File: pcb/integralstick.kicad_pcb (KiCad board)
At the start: 4 copper layers, 235 parts, among them J1 CONN_INTEGRALSTICK_FPGA_DEVICE, J2 CONN_INTEGRALSTICK_MCU_DEVICE, Q1 SSM6N58NU, Q2 SSM6N58NU, Q3 SSM6N58NU, U1 STM32F777NIH6‎, U10 DSC6083MI2A-032K768, U12 DSC6001HI2A-025.0000‎, U2 XC7A50T-1FTG256C, U3 S27KS0641, U4 S27KS0641, U5 KSZ9031RN, U6 S25FL064LABNFI011‎, U7 LTC3374-QFN, U8 DSC6001HI2A-025.0000, U9 AT24MAC402-UDFN

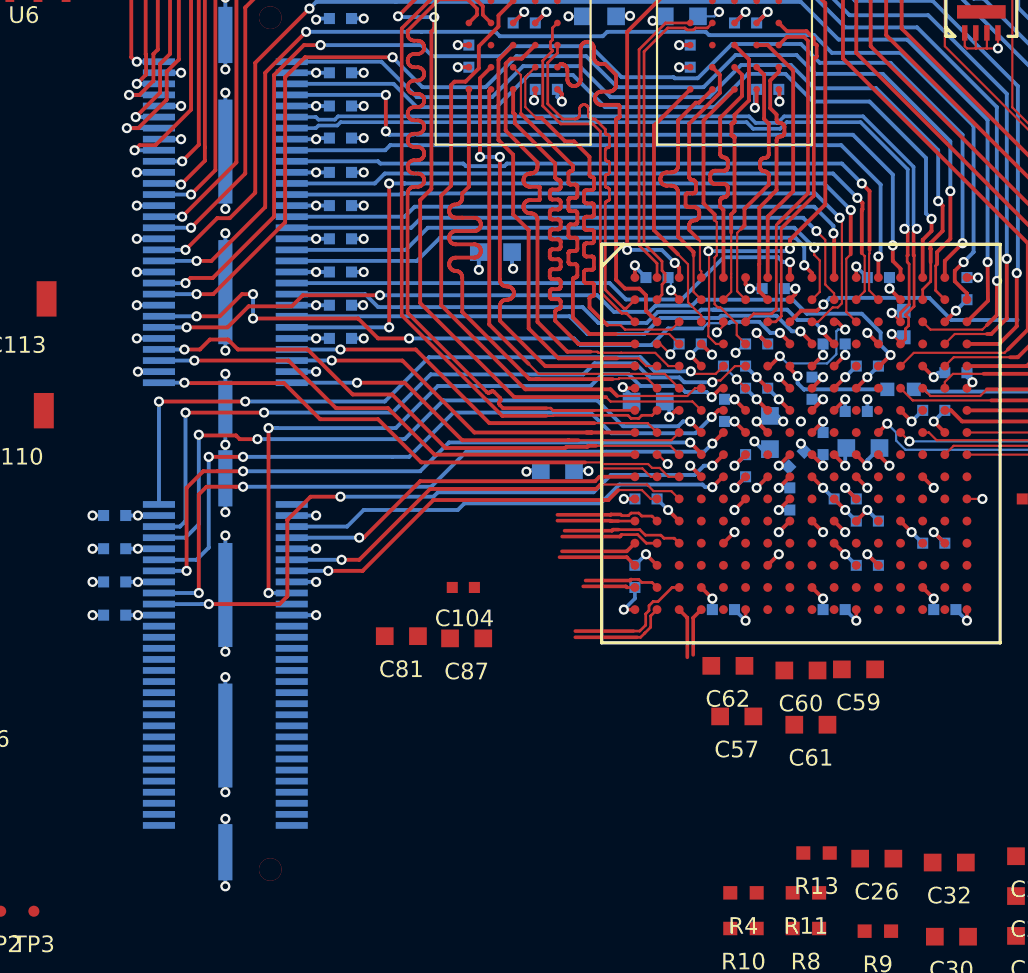
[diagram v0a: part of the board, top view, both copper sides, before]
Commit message: Initial layout of LVDS bank
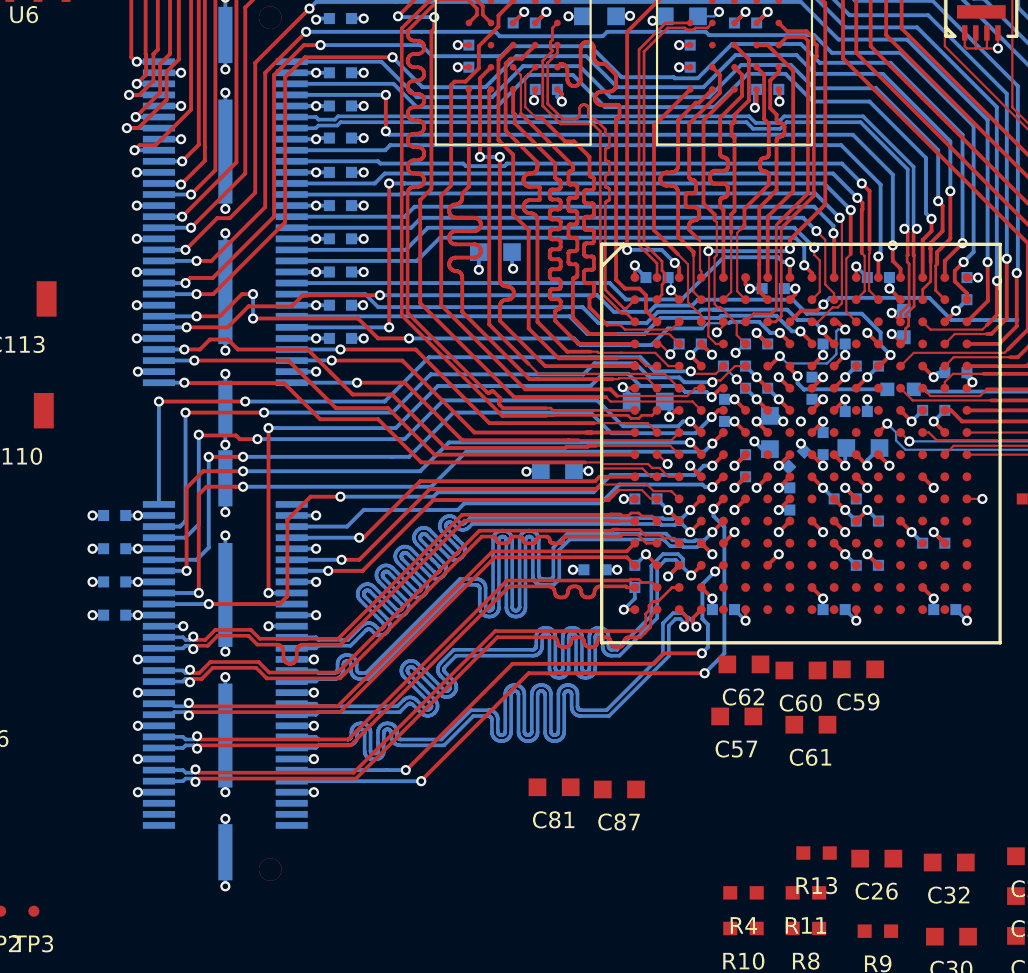
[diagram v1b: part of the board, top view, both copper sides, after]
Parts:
- C104: moved to B.Cu
- moved C87 9.71 mm to (55.8, 58.6)
- moved C81 9.71 mm to (52.9, 58.5)
- moved C104 6.00 mm to (54.7, 48.7)
- moved C62 0.73 mm to (61.4, 53.0)
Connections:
- J1 pad 10: /FPGA/LVDS_DQ4_N -> /FPGA/LVDS_DQ8_N
- J1 pad 11: /FPGA/LVDS_DQ2_P -> /FPGA/GPIO_2V5_0
- J1 pad 12: /FPGA/LVDS_DQ2_N -> /FPGA/LVDS_DQ8_P
- J1 pad 15: /FPGA/LVDS_DQ8_P -> /FPGA/LVDS_DQ7_N
- J1 pad 16: /FPGA/GPIO_2V5_0 -> /FPGA/LVDS_DQ6_N
- J1 pad 17: /FPGA/LVDS_DQ8_N -> /FPGA/LVDS_DQ7_P
- J1 pad 18: /FPGA/GPIO_2V5_1 -> /FPGA/LVDS_DQ6_P
- J1 pad 2: /2V5 -> /Power Supply/5V0
- J1 pad 21: /FPGA/LVDS_DQ6_P -> /FPGA/LVDS_DQ5_N
- J1 pad 22: /FPGA/LVDS_DQ5_P -> /FPGA/LVDS_DQ4_N
- J1 pad 23: /FPGA/LVDS_DQ6_N -> /FPGA/LVDS_DQ5_P
- J1 pad 24: /FPGA/LVDS_DQ5_N -> /FPGA/LVDS_DQ4_P
- J1 pad 25: /1V8 -> /2V5
- J1 pad 27: /FPGA/LVDS_DQ7_P -> /FPGA/LVDS_DQ3_N
- J1 pad 28: /FPGA/LVDS_DQ7_N -> /FPGA/LVDS_DQ2_N
- J1 pad 29: /FPGA/LVDS_DQ3_N -> /FPGA/LVDS_DQ3_P
- J1 pad 3: /2V5 -> /Power Supply/5V0
- J1 pad 30: /FPGA/LVDS_DQ3_P -> /FPGA/LVDS_DQ2_P
- J1 pad 33: /1V8 -> /FPGA/LVDS_DQ1_N
- J1 pad 34: /2V5 -> /FPGA/LVDS_DQ0_N
- J1 pad 35: /FPGA/LVDS_DQ0_P -> /FPGA/LVDS_DQ1_P
- J1 pad 36: /FPGA/LVDS_DQ1_P -> /FPGA/LVDS_DQ0_P
- J1 pad 37: /FPGA/LVDS_DQ0_N -> /2V5
- J1 pad 38: /FPGA/LVDS_DQ1_N -> /2V5
- J1 pad 9: /FPGA/LVDS_DQ4_P -> /FPGA/GPIO_2V5_1
- U2 pad L4: /FPGA/LVDS_DQ0_P -> /FPGA/LVDS_DQ1_P
- U2 pad L5: /FPGA/GPIO_2V5_0 -> /FPGA/GPIO_2V5_1
- U2 pad M1: /FPGA/LVDS_DQ1_N -> /FPGA/LVDS_DQ0_N
- U2 pad M2: /FPGA/LVDS_DQ1_P -> /FPGA/LVDS_DQ0_P
- U2 pad M4: /FPGA/LVDS_DQ0_N -> /FPGA/LVDS_DQ1_N
- U2 pad M5: /FPGA/LVDS_DQ5_P -> /FPGA/LVDS_DQ3_P
- U2 pad N1: /FPGA/LVDS_DQ3_P -> /FPGA/LVDS_DQ4_P
- U2 pad N4: /FPGA/LVDS_DQ5_N -> /FPGA/LVDS_DQ3_N
- U2 pad P1: /FPGA/LVDS_DQ3_N -> /FPGA/LVDS_DQ4_N
- U2 pad P3: /FPGA/LVDS_DQ4_N -> /FPGA/LVDS_DQ5_N
- U2 pad P4: /FPGA/LVDS_DQ4_P -> /FPGA/LVDS_DQ5_P
- U2 pad P5: /FPGA/GPIO_2V5_1 -> /FPGA/GPIO_2V5_0
- U2 pad R3: /FPGA/LVDS_DQ7_P -> /FPGA/LVDS_DQ8_P
- U2 pad T2: /FPGA/LVDS_DQ7_N -> /FPGA/LVDS_DQ8_N
- U2 pad T3: /FPGA/LVDS_DQ8_N -> /FPGA/LVDS_DQ7_N
- U2 pad T4: /FPGA/LVDS_DQ8_P -> /FPGA/LVDS_DQ7_P
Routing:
- net /2V5: track 12.5 -> 50.6 mm, vias 3 -> 16
- net /FPGA/LVDS_DQ5_P: track 0.00 -> 37.8 mm, vias 0 -> 1
- net /FPGA/LVDS_DQ5_N: track 0.00 -> 37.5 mm, vias 0 -> 1
- net /FPGA/LVDS_DQ3_P: track 3.45 -> 37.8 mm, vias 0 -> 1
- net /FPGA/LVDS_DQ3_N: track 3.56 -> 37.8 mm, vias 0 -> 1
- net /FPGA/LVDS_DQ1_N: track 3.51 -> 37.7 mm, vias 0 -> 1
- net /FPGA/LVDS_DQ1_P: track 4.73 -> 37.7 mm, vias 0 -> 1
- net /FPGA/LVDS_DQ7_N: track 4.51 -> 37.3 mm, vias 0 -> 1
- net /FPGA/LVDS_DQ7_P: track 5.94 -> 37.8 mm, vias 0 -> 1
- net /FPGA/GPIO_2V5_1: track 0.00 -> 29.3 mm, vias 0 -> 3
- net /FPGA/LVDS_DQ0_N: track 0.00 -> 25.6 mm, vias 0 -> 1
- net /FPGA/LVDS_DQ0_P: track 0.00 -> 25.6 mm, vias 0 -> 1
- net /FPGA/LVDS_DQ8_P: track 2.20 -> 27.6 mm, vias 0 -> 1
- net /FPGA/GPIO_2V5_0: track 0.00 -> 25.4 mm, vias 0 -> 3
- net /FPGA/LVDS_DQ8_N: track 2.31 -> 27.6 mm, vias 0 -> 1
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
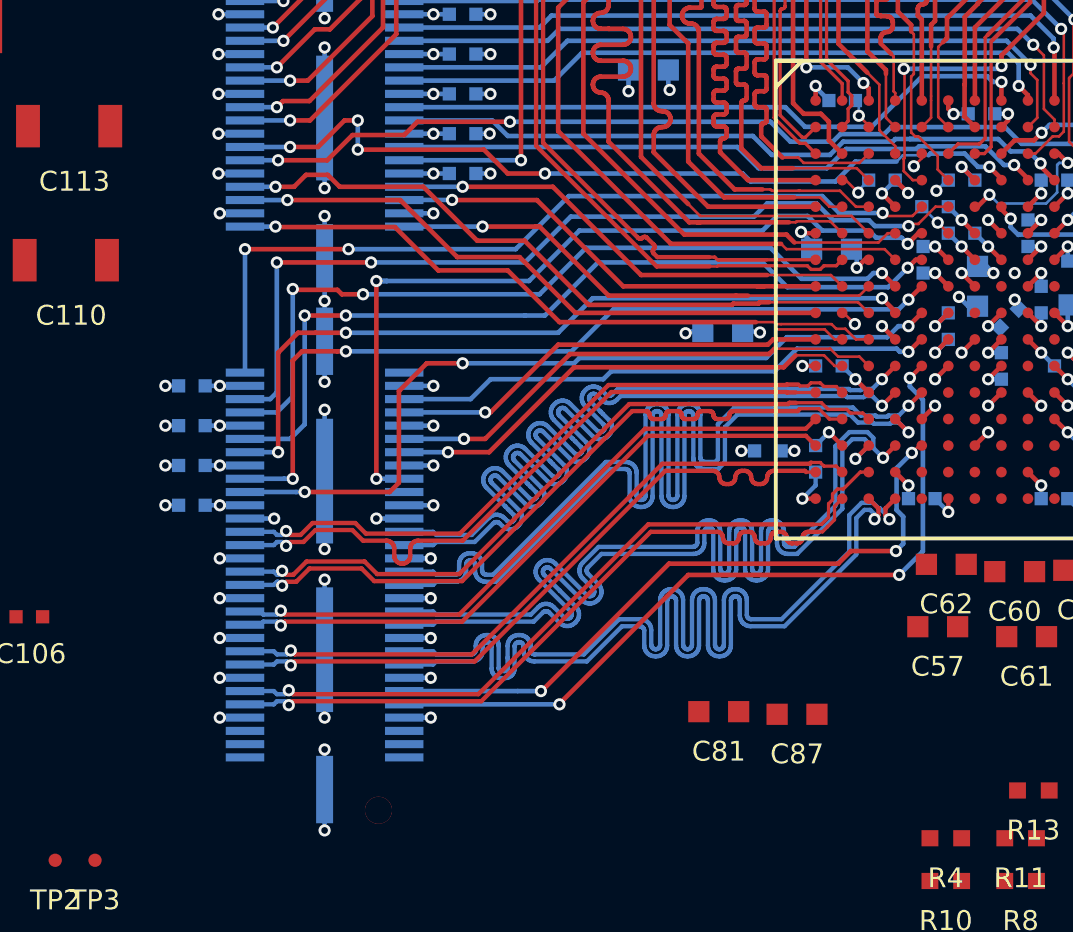
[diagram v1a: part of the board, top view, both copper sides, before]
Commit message: Added missing 1V8 clock. Tweaked planes. Added some layer change caps.
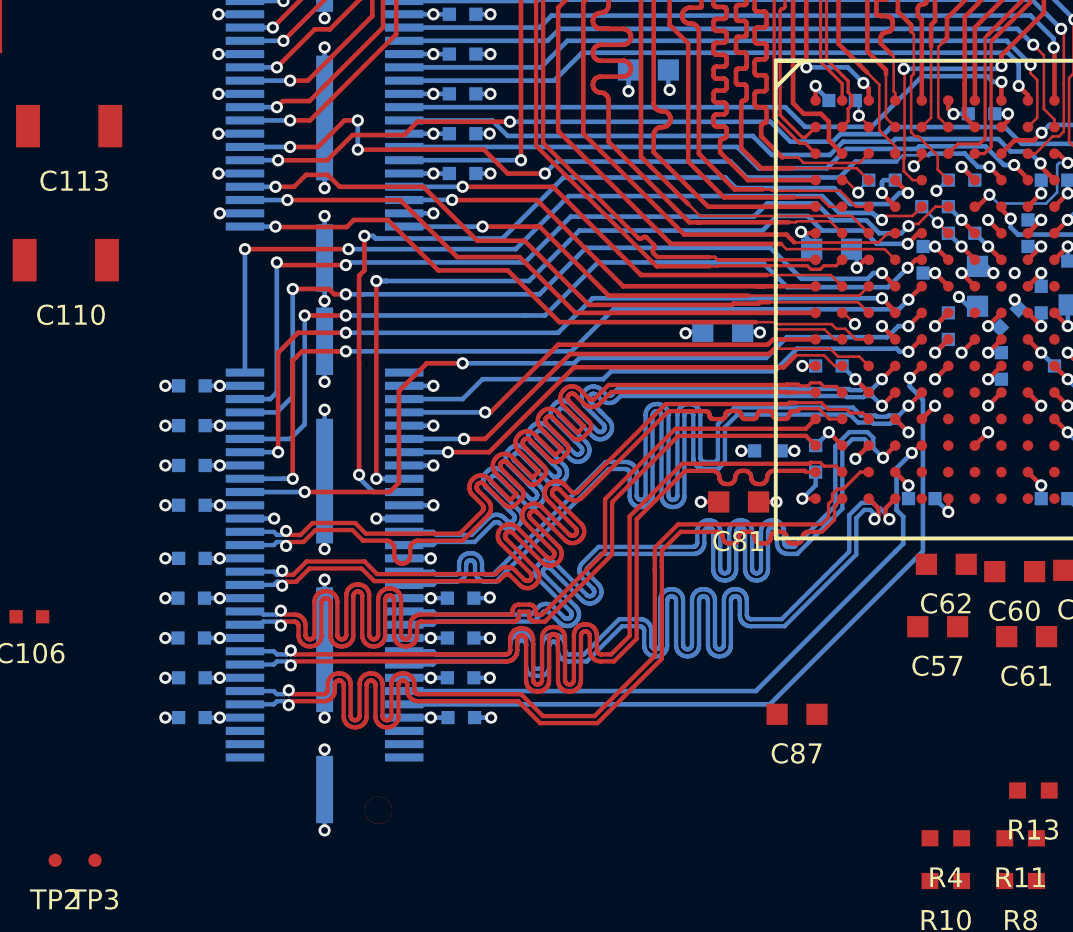
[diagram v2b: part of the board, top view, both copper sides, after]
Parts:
- added C135: 0.47 uF, azonenberg_pcb:EIA_0402_CAP_NOSILK, B.Cu at (33.0, 55.8)
- added C136: 0.47 uF, azonenberg_pcb:EIA_0402_CAP_NOSILK, B.Cu at (33.0, 54.2)
- added C137: 0.47 uF, azonenberg_pcb:EIA_0402_CAP_NOSILK, B.Cu at (33.0, 52.8)
- added C138: 0.47 uF, azonenberg_pcb:EIA_0402_CAP_NOSILK, B.Cu at (33.0, 57.2)
- added C139: 0.47 uF, azonenberg_pcb:EIA_0402_CAP_NOSILK, B.Cu at (33.0, 58.8)
- added C140: 0.47 uF, azonenberg_pcb:EIA_0402_CAP_NOSILK, B.Cu at (43.1, 58.8)
- added C141: 0.47 uF, azonenberg_pcb:EIA_0402_CAP_NOSILK, B.Cu at (43.1, 57.2)
- added C142: 0.47 uF, azonenberg_pcb:EIA_0402_CAP_NOSILK, B.Cu at (43.1, 55.8)
- added C143: 0.47 uF, azonenberg_pcb:EIA_0402_CAP_NOSILK, B.Cu at (43.1, 54.2)
- moved C81 7.94 mm to (53.6, 50.6)
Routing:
- net /RAM/CLK_1V8_1: track 0.68 -> 33.9 mm, vias 1 -> 3
- net /GND: track 385.9 -> 413.0 mm, vias 90 -> 100
- net /2V5: track 50.6 -> 70.6 mm, vias 16 -> 17
- net /FPGA/LVDS_DQ4_P: track 24.7 -> 37.9 mm
- net /FPGA/LVDS_DQ4_N: track 24.7 -> 37.9 mm
- net /FPGA/LVDS_DQ0_P: track 25.6 -> 37.8 mm
- net /FPGA/LVDS_DQ0_N: track 25.6 -> 37.8 mm
- net /FPGA/LVDS_DQ6_P: track 25.8 -> 37.8 mm
- net /FPGA/LVDS_DQ6_N: track 25.8 -> 37.8 mm
- net /FPGA/LVDS_DQ2_N: track 27.0 -> 37.8 mm
- net /FPGA/LVDS_DQ2_P: track 27.0 -> 37.8 mm
- net /FPGA/LVDS_DQ8_N: track 27.6 -> 37.8 mm
- net /FPGA/LVDS_DQ8_P: track 27.6 -> 37.8 mm
- net /FPGA/GPIO_2V5_1: vias 3 -> 1
- net /FPGA/GPIO_2V5_0: vias 3 -> 1

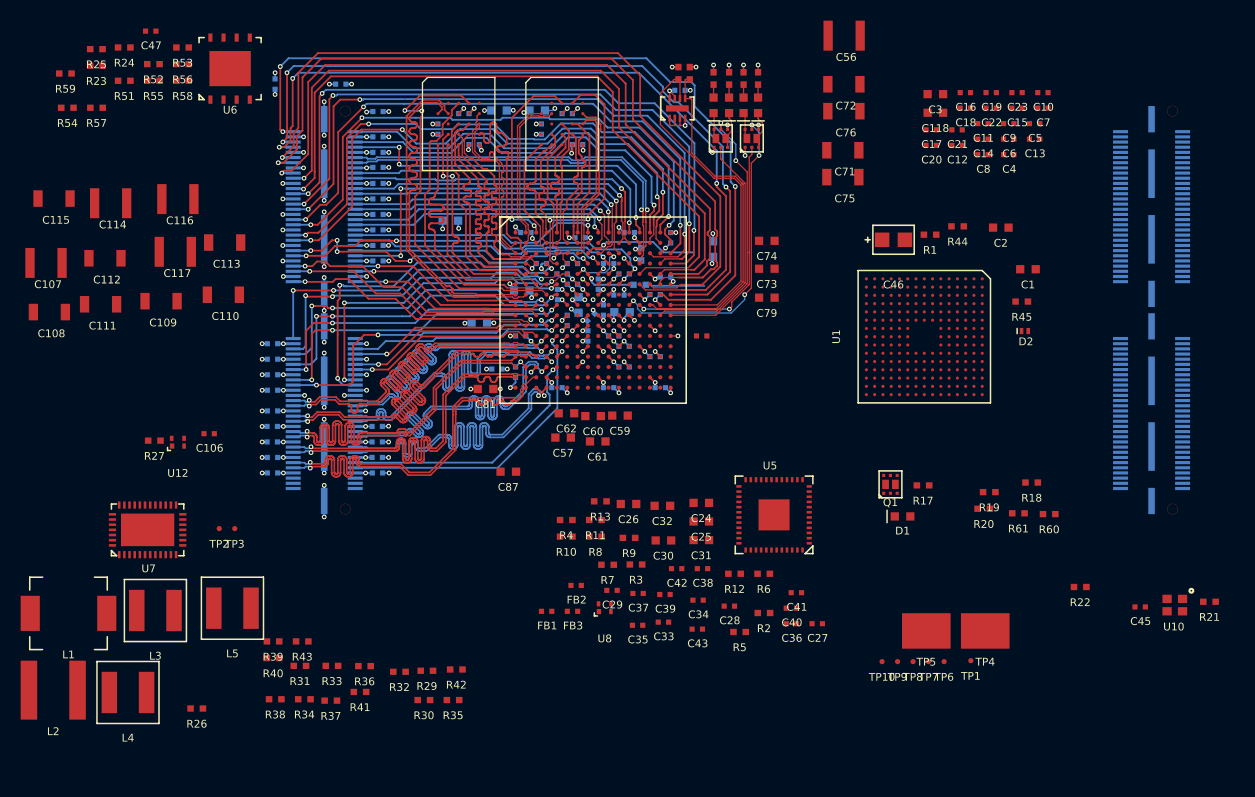
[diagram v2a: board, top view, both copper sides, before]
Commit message: Continued FPGA layout. Fanned out most signals going to MCU but pin assignments aren't final.
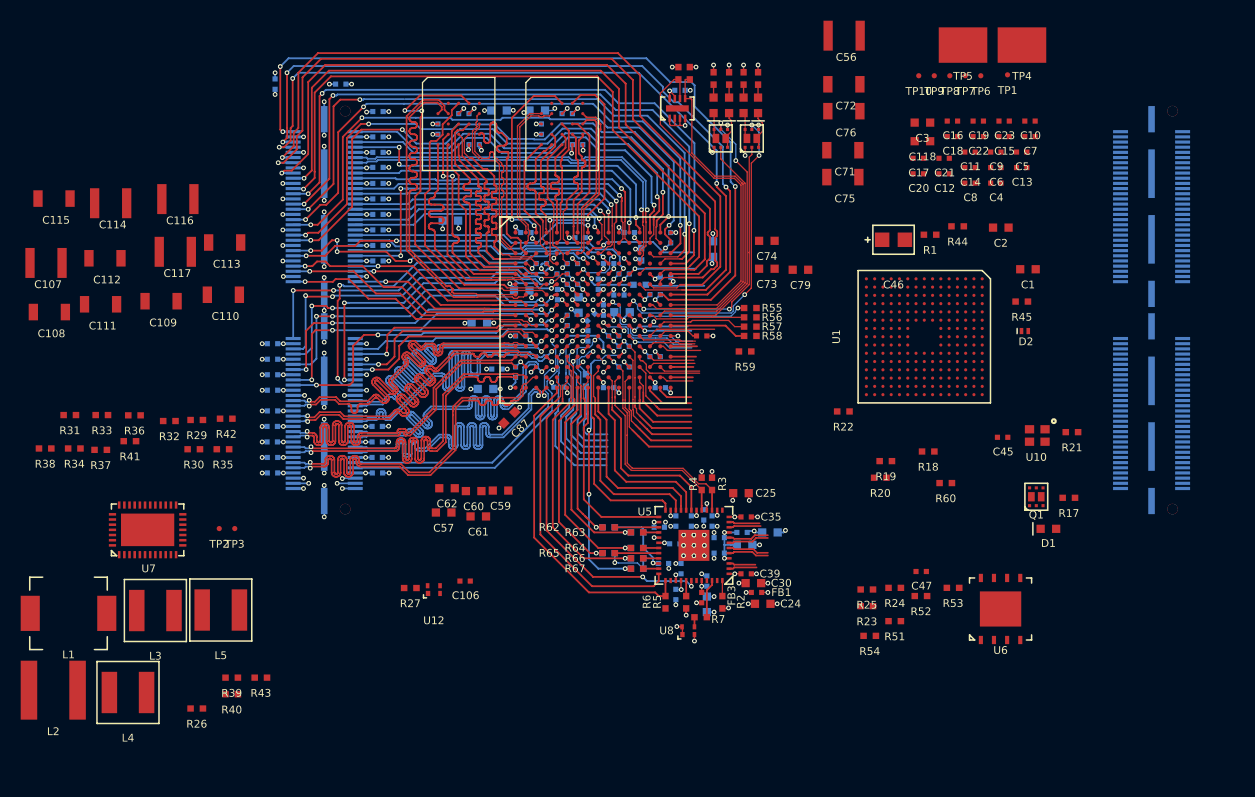
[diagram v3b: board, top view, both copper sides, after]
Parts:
- added R62: 33, azonenberg_pcb:EIA_0402_RES_NOSILK, F.Cu at (65.5, 64.0)
- added R63: 33, azonenberg_pcb:EIA_0402_RES_NOSILK, F.Cu at (68.2, 64.5)
- added R64: 33, azonenberg_pcb:EIA_0402_RES_NOSILK, F.Cu at (68.2, 66.0)
- added R65: 33, azonenberg_pcb:EIA_0402_RES_NOSILK, F.Cu at (65.5, 66.5)
- added R66: 33, azonenberg_pcb:EIA_0402_RES_NOSILK, F.Cu at (68.2, 67.0)
- added R67: 33, azonenberg_pcb:EIA_0402_RES_NOSILK, F.Cu at (68.2, 68.0)
- C26, C27, C28, C29, C31, C32, C33, C34, C36, C37, C38, C40, C41, C42, C43, C81, FB2, R10, R11, R12, R13, R61, R8, R9: moved to B.Cu
- moved R54 92.9 mm to (90.8, 74.5)
- moved C47 91.0 mm to (95.7, 68.3)
- moved R23 91.0 mm to (90.5, 71.6)
- moved R24 91.0 mm to (93.2, 69.9)
- moved R25 91.0 mm to (90.5, 70.0)
- moved R51 91.0 mm to (93.2, 73.1)
- moved R53 91.0 mm to (98.8, 69.9)
- moved U6 91.0 mm to (103.4, 71.9)
- moved R52 90.3 mm to (95.7, 70.7)
- moved R59 71.0 mm to (78.7, 47.0)
- moved R57 66.7 mm to (79.2, 44.6)
- moved R55 61.8 mm to (79.2, 42.8)
- moved R58 60.2 mm to (79.2, 45.5)
- moved R56 60.1 mm to (79.2, 43.7)
- moved TP1 56.8 mm to (104.1, 20.2)
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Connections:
- U2 pad E11: /FPGA/FPGA_CLK_25MHZ -> /FPGA/CLK_3V3_1
- U2 pad E12: /FPGA/CLK_3V3_1 -> /FPGA/FPGA_CLK_25MHZ
- U2 pad M6: /Ethernet/RGMII_TXD2 -> /MCU/DCMI_D7
- U2 pad N11: /MCU/RMII_REFCLK -> /Ethernet/RGMII_RX_CLK
- U2 pad N12: /Ethernet/RGMII_MDC -> /MCU/SPI5_SCK
- U2 pad N13: /Ethernet/RGMII_RXD2 -> /MCU/DCMI_D0
- U2 pad N14: /Ethernet/RGMII_RX_CLK -> /MCU/RMII_REFCLK
- U2 pad N6: /Ethernet/RGMII_TXD1 -> /Ethernet/RGMII_RXD0
- U2 pad P10: /Ethernet/RGMII_RST_N -> /MCU/DCMI_D4
- U2 pad P11: /ETH_LED1_N -> /ETH_LED2_N
- U2 pad P13: /Ethernet/RGMII_RXD3 -> /MCU/DCMI_D2
- U2 pad P14: /Ethernet/RGMII_RX_DV -> /MCU/DCMI_D3
- U2 pad P15: /Ethernet/RGMII_MDIO -> /MCU/DCMI_D1
- U2 pad P6: /MCU/DCMI_D7 -> /Ethernet/RGMII_RX_DV
- U2 pad P8: /Ethernet/RGMII_TXD0 -> /Ethernet/RGMII_TX_CLK
- U2 pad R10: Net-(R22-Pad1) -> /Ethernet/RGMII_TXD0
- U2 pad R11: /MCU/SPI5_SCK -> /ETH_LED1_N
- U2 pad R12: /ETH_LED2_N -> /MCU/DCMI_PIXCLK
- U2 pad R16: /MCU/DCMI_PIXCLK -> Net-(R22-Pad1)
- U2 pad R5: /MCU/DCMI_D3 -> /Ethernet/RGMII_MDC
- U2 pad R6: /MCU/DCMI_D5 -> /Ethernet/RGMII_RST_N
- U2 pad R7: /MCU/DCMI_D6 -> /Ethernet/RGMII_RXD2
- U2 pad R8: /Ethernet/RGMII_TX_EN -> /Ethernet/RGMII_RXD3
- U2 pad T10: /MCU/DCMI_D2 -> /Ethernet/RGMII_TXD1
- U2 pad T14: /Ethernet/RGMII_RXD0 -> /MCU/DCMI_D6
- U2 pad T15: /Ethernet/RGMII_RXD1 -> /MCU/DCMI_D5
- U2 pad T5: /MCU/DCMI_D4 -> /Ethernet/RGMII_MDIO
- U2 pad T7: /Ethernet/RGMII_TX_CLK -> /Ethernet/RGMII_RXD1
- U2 pad T8: /MCU/DCMI_D0 -> /Ethernet/RGMII_TX_EN
- U2 pad T9: /MCU/DCMI_D1 -> /Ethernet/RGMII_TXD2
- U5 pad 27: /Ethernet/RGMII_RXD3 -> Net-(R62-Pad2)
- U5 pad 28: /Ethernet/RGMII_RXD2 -> Net-(R63-Pad2)
- U5 pad 31: /Ethernet/RGMII_RXD1 -> Net-(R64-Pad2)
- U5 pad 32: /Ethernet/RGMII_RXD0 -> Net-(R65-Pad2)
- U5 pad 33: /Ethernet/RGMII_RX_DV -> Net-(R66-Pad2)
- U5 pad 35: /Ethernet/RGMII_RX_CLK -> Net-(R67-Pad2)
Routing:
- net /GND: track 413.0 -> 525.4 mm, vias 100 -> 135
- net /2V5: track 70.6 -> 146.5 mm, vias 17 -> 20
- net /3V3: track 170.8 -> 218.1 mm, vias 44 -> 51
- net /Ethernet/RGMII_RST_N: track 0.00 -> 32.4 mm, vias 0 -> 2
- net /Ethernet/RGMII_MDIO: track 0.00 -> 32.0 mm
- net /Ethernet/RGMII_MDC: track 0.00 -> 30.6 mm
- net /1V2: track 0.00 -> 30.0 mm, vias 0 -> 8
- net /Ethernet/RGMII_RX_CLK: track 0.00 -> 28.4 mm, vias 0 -> 4
- net /Ethernet/RGMII_RX_DV: track 0.00 -> 25.7 mm, vias 0 -> 1
- net /Ethernet/RGMII_RXD0: track 0.00 -> 23.0 mm, vias 0 -> 1
- net /Ethernet/RGMII_RXD1: track 0.00 -> 21.0 mm, vias 0 -> 1
- net /ETH_LED2_N: track 0.00 -> 20.9 mm
- net /Ethernet/RGMII_RXD2: track 0.00 -> 20.6 mm, vias 0 -> 1
- net /Ethernet/RGMII_TXD3: track 0.00 -> 20.5 mm
- net /Ethernet/RGMII_TX_CLK: track 0.00 -> 19.9 mm
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- added copper zone on In2.Cu, net /Power Supply/5V0
